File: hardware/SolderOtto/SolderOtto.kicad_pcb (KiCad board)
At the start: 4 copper layers, 120 x 60 mm, 226 parts, among them J201 Conn_02x04_Counter_Clockwise, J301 TC-2050, J401 Conn_01x20, J501 Conn_01x08, J601 Conn_01x07, P301 USB_C_Plug_USB2.0, Q201 T2N7002AK, Q202 BC858B, Q203 BC847A, Q204 BC847A, Q801 Q_Dual_NMOS, Q802 Q_Dual_NMOS, Q803 Q_Dual_NMOS, Q804 DTD123EK, Q805 DTD123EK, Q806 DTD123EK, Q807 Q_Dual_NMOS, Q808 Q_Dual_NMOS, Q809 DTD123EK, Q810 DTD123EK, Q901 BC847A, Q902 BC858B, Q903 BC847A, SW301 SW_Push, U201 LM5012, U202 AP3211K, U203 AP3211K, U204 AP3211K, U205 LM27761, U206 MCP9701T-E/TT, U301 USBLC6-2SC6, U302 STM32G474QETx, U303 MX25R3235FM1xx0, U701 SN74LVC125A, U702 TS5A3159ADCK, U801 VOM1271, U802 VOM1271, U803 VOM1271, U804 VOM1271, U805 VOM1271, U901 OPA202, U902 LM358B, U903 74hc4053, U904 OPA202, U905 OPA202, Y301 32.768 kHz

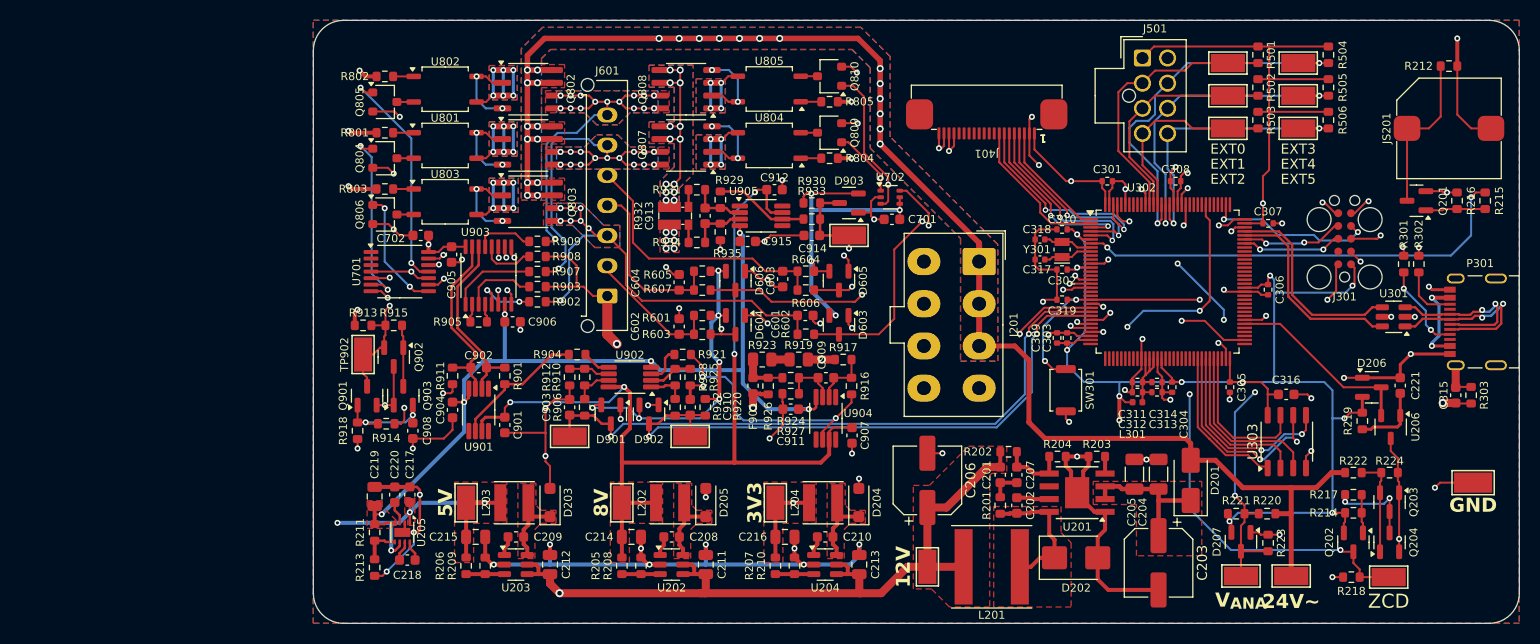
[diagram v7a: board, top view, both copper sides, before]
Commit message: fix drc findings
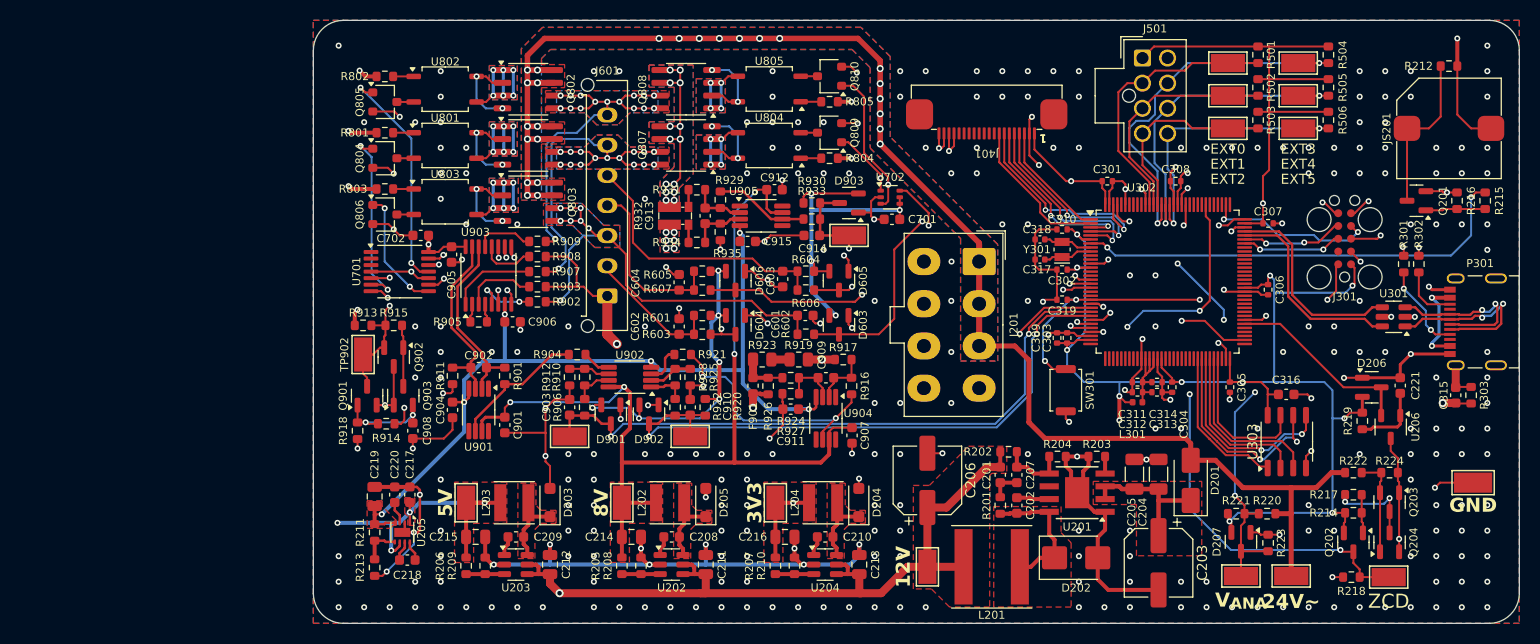
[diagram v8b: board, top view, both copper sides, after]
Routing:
- net GND: vias 84 -> 318
- added copper zone on In2.Cu, net GND
